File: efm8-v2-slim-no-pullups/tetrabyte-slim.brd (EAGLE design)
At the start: 31.8 x 76.2 mm, 18 parts, among them J1 TYPE-C-31-M-12, U1 EFM8UB20F64G-B-QFP48

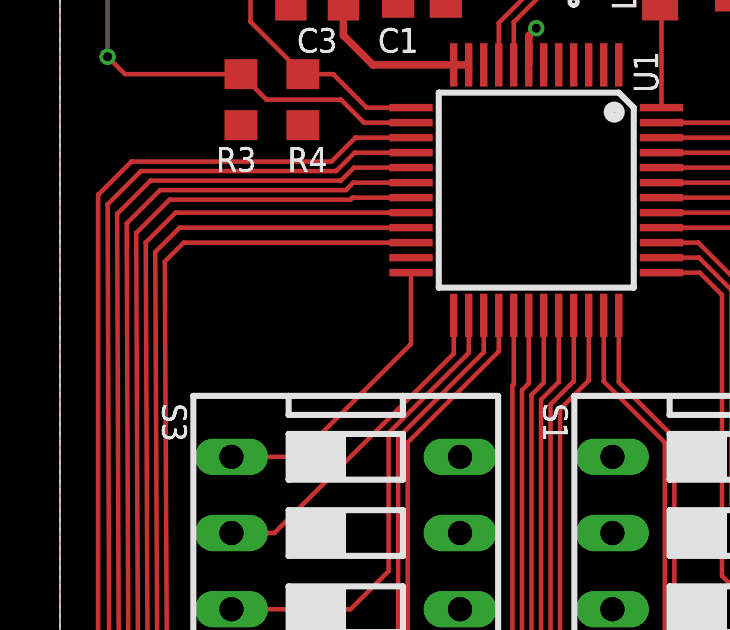
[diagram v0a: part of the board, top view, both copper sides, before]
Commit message: add bootload switch
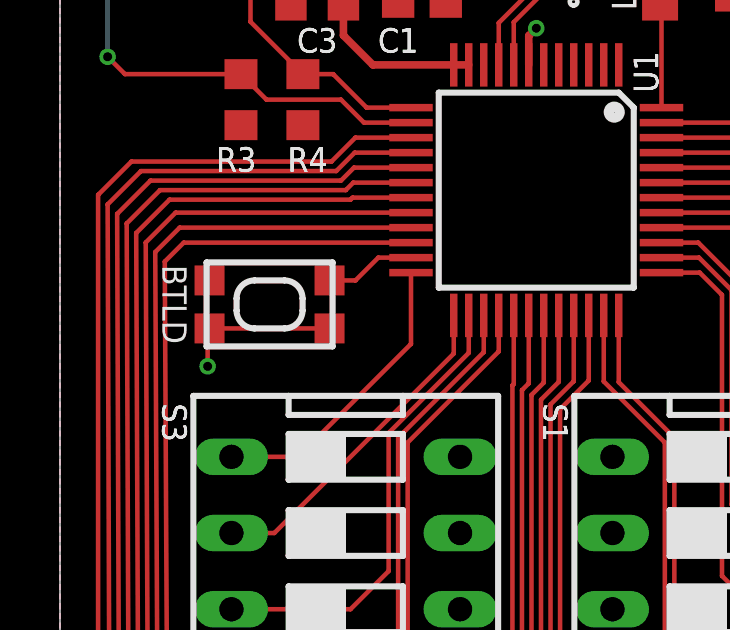
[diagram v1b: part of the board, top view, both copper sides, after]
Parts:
- added SW1: KMR211NGLFS, adafruit:KMR2
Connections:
- net BTLD: now also SW1.1
- net GND: now also SW1.2, SW1.4
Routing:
- net GND: track 14.1 -> 19.4 mm, vias 10 -> 11
- net BTLD: track 0.00 -> 3.03 mm
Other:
- board text added: "BTLD"
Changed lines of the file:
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@@
 <circle x="29.845" y="74.295" radius="2.31" width="0.0254" layer="48"/>
 <circle x="1.905" y="74.295" radius="2.31" width="0.0254" layer="48"/>
+<wire x1="9.084996875" y1="49.400003125" x2="4.885003125" y2="49.400003125" width="0.2032" layer="121"/>
+<wire x1="4.885003125" y1="49.400003125" x2="4.885003125" y2="52.199996875" width="0.2032" layer="121"/>
+<wire x1="4.885003125" y1="52.199996875" x2="9.084996875" y2="52.199996875" width="0.2032" layer="121"/>
+<wire x1="9.084996875" y1="52.199996875" x2="9.084996875" y2="49.400003125" width="0.2032" layer="121"/>
+<wire x1="8.084996875" y1="51" x2="7.485" y2="51.599996875" width="0.2032" layer="121" curve="90"/>
+<wire x1="8.084996875" y1="51" x2="8.084996875" y2="50.6" width="0.2032" layer="121"/>
+<wire x1="7.485" y1="50.000003125" x2="8.085" y2="50.6" width="0.2032" layer="121" curve="89.999702"/>
+<wire x1="7.485" y1="50.000003125" x2="6.485" y2="50.000003125" width="0.2032" layer="121"/>
+<wire x1="5.885003125" y1="50.6" x2="6.485" y2="50" width="0.2032" layer="121" curve="89.999702"/>
+<wire x1="5.885003125" y1="50.6" x2="5.885003125" y2="51" width="0.2032" layer="121"/>
+<wire x1="6.485" y1="51.599996875" x2="5.885003125" y2="51" width="0.2032" layer="121" curve="90"/>
+<wire x1="6.485" y1="51.599996875" x2="7.485" y2="51.599996875" width="0.2032" layer="121"/>
+<text x="4.22275" y="50.8" size="0.8128" layer="121" font="vector" ratio="16" rot="SR270" align="top-center">BTLD</text>
 </plain>
 <attributes>
@@
 <attribute name="NAME" x="4.22275" y="23.368" size="0.8128" layer="25" font="vector" ratio="16" rot="SR270" align="top-left"/>
 </element>
+<element name="SW1" library="adafruit" package="KMR2" value="KMR211NGLFS " x="6.985" y="50.8"/>
 </elements>
 <signals>
@@
 <contactref element="S2" pad="7"/>
 <contactref element="S2" pad="8"/>
+<contactref element="SW1" pad="2"/>
+<contactref element="SW1" pad="4"/>
+<wire x1="4.985" y1="50" x2="8.985" y2="50" width="0.1524" layer="1"/>
+<via x="4.92125" y="48.73625" extent="1-16" drill="0.3"/>
+<wire x1="4.92125" y1="48.73625" x2="4.92125" y2="49.93625" width="0.1524" layer="1"/>
+<wire x1="4.92125" y1="49.93625" x2="4.985" y2="50" width="0.1524" layer="1"/>
 </signal>
 <signal name="NRESET">
@@
 <wire x1="6.35" y1="60.2225" x2="8.09625" y2="58.47625" width="0.1524" layer="1"/>
 </signal>
-<signal name="BTLD">
-<contactref element="U1" pad="23"/>
-</signal>
 <signal name="S3-2">
 <contactref element="S3" pad="2"/>
@@
 <wire x1="4.1275" y1="21.59" x2="5.715" y2="21.59" width="0.1524" layer="1"/>
 </signal>
+<signal name="BTLD">
+<contactref element="SW1" pad="1"/>
+<contactref element="U1" pad="23"/>
+<wire x1="8.985" y1="51.6" x2="9.84875" y2="51.6" width="0.1524" layer="1"/>
+<wire x1="9.84875" y1="51.6" x2="10.60875" y2="52.36" width="0.1524" layer="1"/>
+<wire x1="11.7" y1="52.36" x2="10.60875" y2="52.36" width="0.1524" layer="1"/>
+</signal>
 </signals>
